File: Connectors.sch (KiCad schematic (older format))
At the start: 4 parts

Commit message: Arranged symbols
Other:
- moved on the sheet: J?
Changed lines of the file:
@@
 L Connector_Generic:Conn_01x09 J?
 U 1 1 5CE3D253
-P 5175 2850
-F 0 "J?" H 5255 2892 50  0000 L CNN
-F 1 "Conn_01x09" H 5255 2801 50  0000 L CNN
-F 2 "" H 5175 2850 50  0001 C CNN
-F 3 "~" H 5175 2850 50  0001 C CNN
-	1    5175 2850
+P 4825 3750
+F 0 "J?" H 4905 3792 50  0000 L CNN
+F 1 "Conn_01x09" H 4905 3701 50  0000 L CNN
+F 2 "" H 4825 3750 50  0001 C CNN
+F 3 "~" H 4825 3750 50  0001 C CNN
+	1    4825 3750
 	1    0    0    -1
 $EndComp
@@
 L Connector_Generic:Conn_02x03_Odd_Even J?
 U 1 1 5CE3EBBD
-P 5150 3800
-F 0 "J?" H 5200 4117 50  0000 C CNN
-F 1 "Conn_02x03_Odd_Even" H 5200 4026 50  0000 C CNN
-F 2 "" H 5150 3800 50  0001 C CNN
-F 3 "~" H 5150 3800 50  0001 C CNN
-	1    5150 3800
+P 5900 4000
+F 0 "J?" H 5950 4317 50  0000 C CNN
+F 1 "Conn_02x03_Odd_Even" H 5950 4226 50  0000 C CNN
+F 2 "" H 5900 4000 50  0001 C CNN
+F 3 "~" H 5900 4000 50  0001 C CNN
+	1    5900 4000
 	1    0    0    -1
 $EndComp
@@
 L Connector_Generic:Conn_01x04 J?
 U 1 1 5CE40335
-P 5925 3400
-F 0 "J?" H 6005 3392 50  0000 L CNN
-F 1 "Conn_01x04" H 6005 3301 50  0000 L CNN
-F 2 "" H 5925 3400 50  0001 C CNN
-F 3 "~" H 5925 3400 50  0001 C CNN
-	1    5925 3400
+P 4850 2600
+F 0 "J?" H 4930 2592 50  0000 L CNN
+F 1 "Conn_01x04" H 4930 2501 50  0000 L CNN
+F 2 "" H 4850 2600 50  0001 C CNN
+F 3 "~" H 4850 2600 50  0001 C CNN
+	1    4850 2600
 	1    0    0    -1
 $EndComp

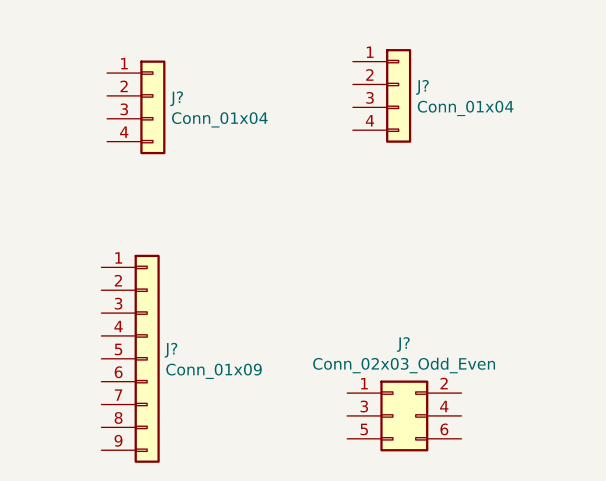
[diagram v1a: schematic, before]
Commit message: Completed associations and added component values
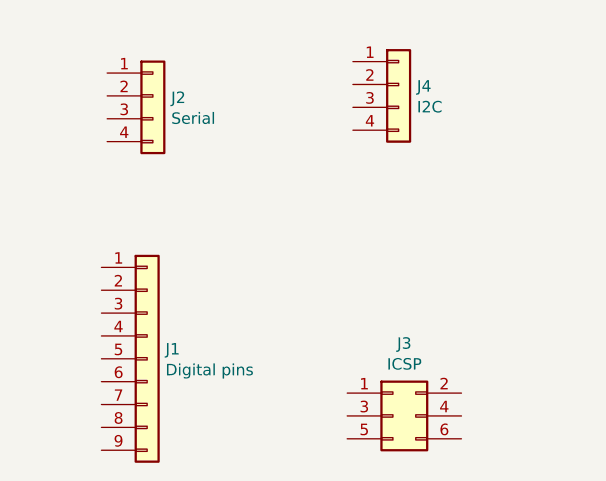
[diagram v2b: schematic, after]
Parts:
- J1: renamed from J?; value Conn_01x09 -> Digital pins; footprint (none) -> Connector_PinHeader_2.54mm:PinHeader_1x09_P2.54mm_Vertical
- J2: renamed from J?; value Conn_01x04 -> Serial; footprint (none) -> Connector_PinHeader_2.54mm:PinHeader_1x04_P2.54mm_Vertical
- J3: renamed from J?; value Conn_02x03_Odd_Even -> ICSP; footprint (none) -> Connector_PinHeader_2.54mm:PinHeader_2x03_P2.54mm_Vertical
- J4: renamed from J?; value Conn_01x04 -> I2C; footprint (none) -> Connector_PinHeader_2.54mm:PinHeader_1x04_P2.54mm_Vertical
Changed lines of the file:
@@
 $EndDescr
 $Comp
-L Connector_Generic:Conn_01x09 J?
+L Connector_Generic:Conn_01x09 J1
 U 1 1 5CE3D253
 P 4825 3750
-F 0 "J?" H 4905 3792 50  0000 L CNN
-F 1 "Conn_01x09" H 4905 3701 50  0000 L CNN
-F 2 "" H 4825 3750 50  0001 C CNN
+F 0 "J1" H 4905 3792 50  0000 L CNN
+F 1 "Digital pins" H 4905 3701 50  0000 L CNN
+F 2 "Connector_PinHeader_2.54mm:PinHeader_1x09_P2.54mm_Vertical" H 4825 3750 50  0001 C CNN
 F 3 "~" H 4825 3750 50  0001 C CNN
 	1    4825 3750
@@
 $EndComp
 $Comp
-L Connector_Generic:Conn_01x04 J?
+L Connector_Generic:Conn_01x04 J4
 U 1 1 5CE3DCFD
 P 5925 2550
-F 0 "J?" H 6005 2542 50  0000 L CNN
-F 1 "Conn_01x04" H 6005 2451 50  0000 L CNN
-F 2 "" H 5925 2550 50  0001 C CNN
+F 0 "J4" H 6005 2542 50  0000 L CNN
+F 1 "I2C" H 6005 2451 50  0000 L CNN
+F 2 "Connector_PinHeader_2.54mm:PinHeader_1x04_P2.54mm_Vertical" H 5925 2550 50  0001 C CNN
 F 3 "~" H 5925 2550 50  0001 C CNN
 	1    5925 2550
@@
 $EndComp
 $Comp
-L Connector_Generic:Conn_02x03_Odd_Even J?
+L Connector_Generic:Conn_02x03_Odd_Even J3
 U 1 1 5CE3EBBD
 P 5900 4000
-F 0 "J?" H 5950 4317 50  0000 C CNN
-F 1 "Conn_02x03_Odd_Even" H 5950 4226 50  0000 C CNN
-F 2 "" H 5900 4000 50  0001 C CNN
+F 0 "J3" H 5950 4317 50  0000 C CNN
+F 1 "ICSP" H 5950 4226 50  0000 C CNN
+F 2 "Connector_PinHeader_2.54mm:PinHeader_2x03_P2.54mm_Vertical" H 5900 4000 50  0001 C CNN
 F 3 "~" H 5900 4000 50  0001 C CNN
 	1    5900 4000
@@
 $EndComp
 $Comp
-L Connector_Generic:Conn_01x04 J?
+L Connector_Generic:Conn_01x04 J2
 U 1 1 5CE40335
 P 4850 2600
-F 0 "J?" H 4930 2592 50  0000 L CNN
-F 1 "Conn_01x04" H 4930 2501 50  0000 L CNN
-F 2 "" H 4850 2600 50  0001 C CNN
+F 0 "J2" H 4930 2592 50  0000 L CNN
+F 1 "Serial" H 4930 2501 50  0000 L CNN
+F 2 "Connector_PinHeader_2.54mm:PinHeader_1x04_P2.54mm_Vertical" H 4850 2600 50  0001 C CNN
 F 3 "~" H 4850 2600 50  0001 C CNN
 	1    4850 2600

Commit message: Finished the hiearchical labels and pins
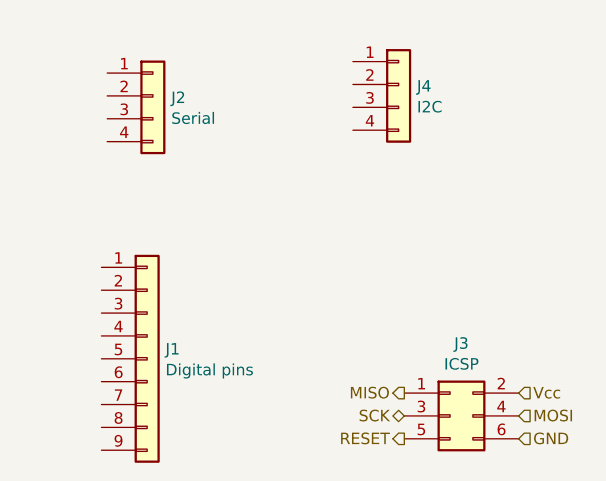
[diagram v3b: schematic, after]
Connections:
- net MISO: now reaches J3.1 (Pin_1)
- net Vcc: now reaches J3.2 (Pin_2)
- net SCK: now reaches J3.3 (Pin_3)
- net MOSI: now reaches J3.4 (Pin_4)
- net RESET: now reaches J3.5 (Pin_5)
- net GND: now reaches J3.6 (Pin_6)
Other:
- moved on the sheet: J3
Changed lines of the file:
@@
 L Connector_Generic:Conn_02x03_Odd_Even J3
 U 1 1 5CE3EBBD
-P 5900 4000
-F 0 "J3" H 5950 4317 50  0000 C CNN
-F 1 "ICSP" H 5950 4226 50  0000 C CNN
-F 2 "Connector_PinHeader_2.54mm:PinHeader_2x03_P2.54mm_Vertical" H 5900 4000 50  0001 C CNN
-F 3 "~" H 5900 4000 50  0001 C CNN
-	1    5900 4000
+P 6150 4000
+F 0 "J3" H 6200 4317 50  0000 C CNN
+F 1 "ICSP" H 6200 4226 50  0000 C CNN
+F 2 "Connector_PinHeader_2.54mm:PinHeader_2x03_P2.54mm_Vertical" H 6150 4000 50  0001 C CNN
+F 3 "~" H 6150 4000 50  0001 C CNN
+	1    6150 4000
 	1    0    0    -1
 $EndComp
@@
 	1    0    0    -1
 $EndComp
+Text HLabel 5950 3900 0    50   Output ~ 0
+MISO
+Text HLabel 5950 4000 0    50   BiDi ~ 0
+SCK
+Text HLabel 5950 4100 0    50   Output ~ 0
+RESET
+Text HLabel 6450 3900 2    50   Input ~ 0
+Vcc
+Text HLabel 6450 4000 2    50   Input ~ 0
+MOSI
+Text HLabel 6450 4100 2    50   Input ~ 0
+GND
 $EndSCHEMATC

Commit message: Completed wiring connectors sheet
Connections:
- net GND: now also J1.8 (Pin_8), J2.1 (Pin_1), J4.1 (Pin_1)
- net SCK: now also J4.4 (Pin_4)
- net Vcc: now also J1.9 (Pin_9), J2.2 (Pin_2), J4.2 (Pin_2)
- net D2: now reaches J1.1 (Pin_1)
- net D3: now reaches J1.2 (Pin_2)
- net D4: now reaches J1.3 (Pin_3)
- net D5: now reaches J1.4 (Pin_4)
- net D6: now reaches J1.5 (Pin_5)
- net D7: now reaches J1.6 (Pin_6)
- net D8: now reaches J1.7 (Pin_7)
- net SDA: now reaches J4.3 (Pin_3)
- net RX: now reaches J2.3 (Pin_3)
- net TX: now reaches J2.4 (Pin_4)
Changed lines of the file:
@@
 Text HLabel 6450 4100 2    50   Input ~ 0
 GND
+Text HLabel 4650 2500 0    50   Input ~ 0
+GND
+Text HLabel 4650 2600 0    50   Input ~ 0
+Vcc
+Text HLabel 4650 2700 0    50   Input ~ 0
+RX
+Text HLabel 4650 2800 0    50   Output ~ 0
+TX
+Text HLabel 5725 2450 0    50   Input ~ 0
+GND
+Text HLabel 5725 2550 0    50   Input ~ 0
+Vcc
+Text HLabel 5725 2650 0    50   BiDi ~ 0
+SDA
+Text HLabel 5725 2750 0    50   BiDi ~ 0
+SCK
+Text HLabel 4625 3350 0    50   BiDi ~ 0
+D2
+Text HLabel 4625 3450 0    50   BiDi ~ 0
+D3
+Text HLabel 4625 3550 0    50   BiDi ~ 0
+D4
+Text HLabel 4625 3650 0    50   BiDi ~ 0
+D5
+Text HLabel 4625 3750 0    50   BiDi ~ 0
+D6
+Text HLabel 4625 3850 0    50   BiDi ~ 0
+D7
+Text HLabel 4625 3950 0    50   BiDi ~ 0
+D8
+Text HLabel 4625 4050 0    50   Input ~ 0
+GND
+Text HLabel 4625 4150 0    50   Input ~ 0
+Vcc
 $EndSCHEMATC

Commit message: Added functional block descriptions
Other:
- note added: "N5 - I2C Connector\n"
- note added: "N6 - Serial Connector\n"
- note added: "N7 - GPIO Connector"
- note added: "N8 - SPI Connector"
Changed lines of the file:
@@
 Text HLabel 4625 4150 0    50   Input ~ 0
 Vcc
+Text Notes 5300 2375 2    50   ~ 0
+N6 - Serial Connector\n
+Text Notes 6300 2350 2    50   ~ 0
+N5 - I2C Connector\n
+Text Notes 5300 3250 2    50   ~ 0
+N7 - GPIO Connector
+Text Notes 6500 3575 2    50   ~ 0
+N8 - SPI Connector
 $EndSCHEMATC
